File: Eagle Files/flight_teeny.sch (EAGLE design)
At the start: 21 parts, among them M4 WIRELESS-NRF24L01, Q1 SI2302, Q2 SI2302, Q3 SI2302, Q5 SI2302, U2 GY-521MPU6050

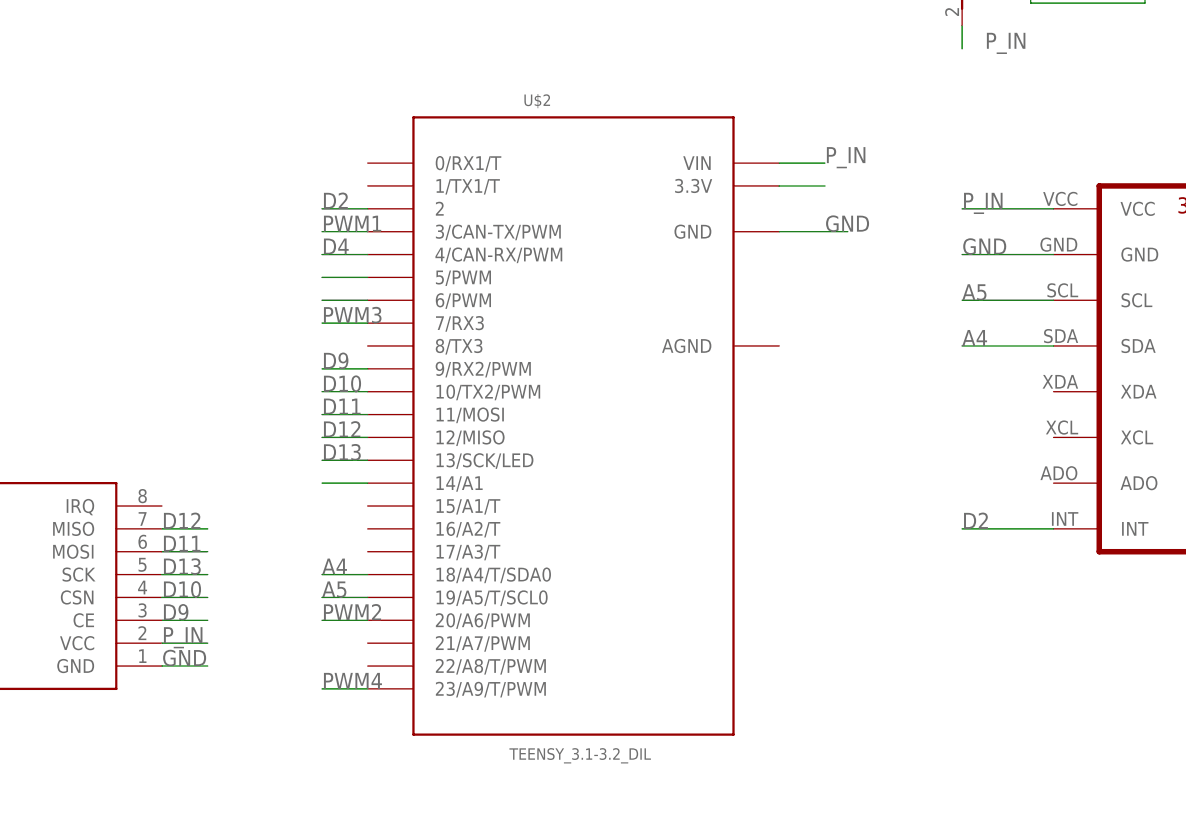
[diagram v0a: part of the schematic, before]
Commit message: Changed power supply for mrf and mpu. Corrected of overlaping pads
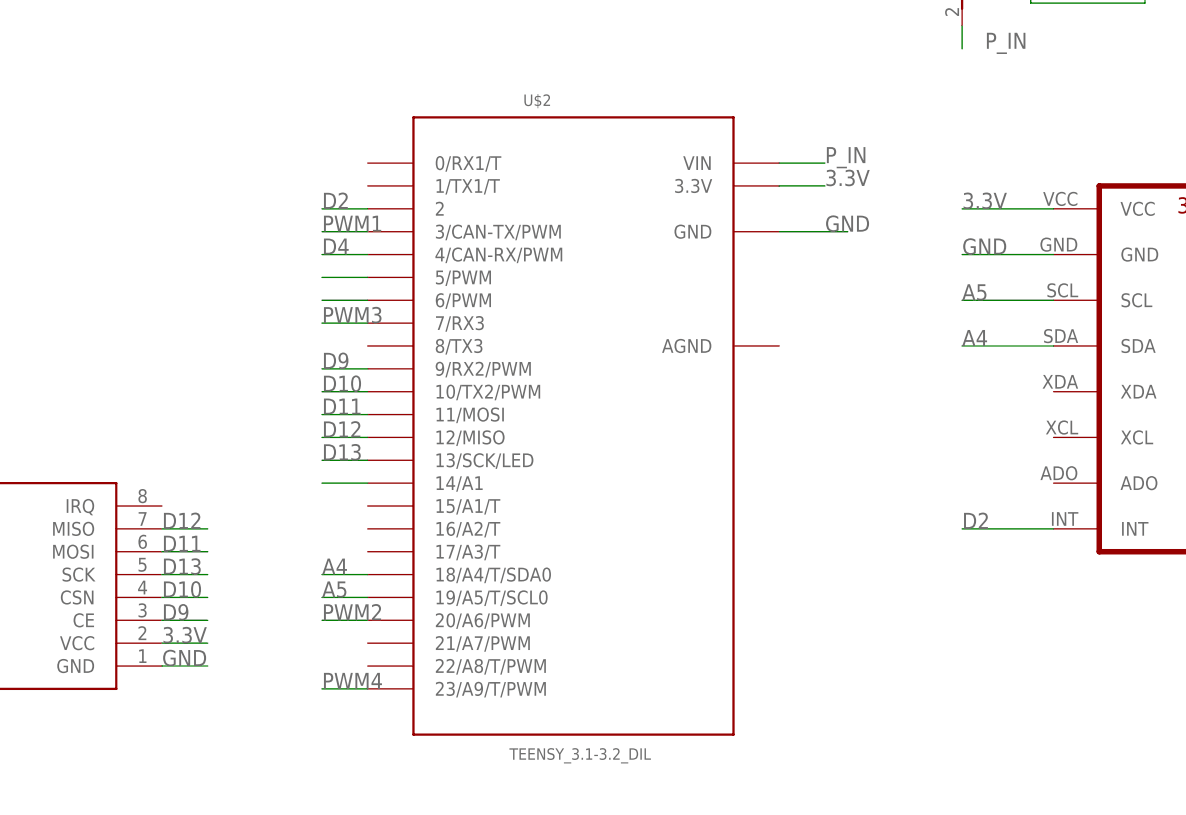
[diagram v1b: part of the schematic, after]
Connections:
- removed net N$10: U$2.3.3V
- new net 3.3V: M4.VCC, U$2.3.3V, U2.VCC
- net P_IN: no longer M4.VCC, U2.VCC
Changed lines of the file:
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@@
 <?xml version="1.0" encoding="utf-8"?>
 <!DOCTYPE eagle SYSTEM "eagle.dtd">
-<eagle version="9.3.2">
+<eagle version="9.2.2">
 <drawing>
 <settings>
@@
 </segment>
 <segment>
+<pinref part="U$2" gate="G$1" pin="VIN"/>
+<wire x1="43.18" y1="-71.12" x2="48.26" y2="-71.12" width="0.1524" layer="91"/>
+<label x="48.26" y="-71.12" size="1.778" layer="95"/>
+</segment>
+</net>
+<net name="N$20" class="0">
+<segment>
+<pinref part="U$2" gate="G$1" pin="14/A1"/>
+<wire x1="-2.54" y1="-106.68" x2="-7.62" y2="-106.68" width="0.1524" layer="91"/>
+</segment>
+</net>
+<net name="3.3V" class="0">
+<segment>
+<pinref part="U$2" gate="G$1" pin="3.3V"/>
+<wire x1="43.18" y1="-73.66" x2="48.26" y2="-73.66" width="0.1524" layer="91"/>
+<label x="48.26" y="-73.66" size="1.778" layer="95"/>
+</segment>
+<segment>
+<pinref part="M4" gate="G$1" pin="VCC"/>
+<wire x1="-25.4" y1="-124.46" x2="-20.32" y2="-124.46" width="0.1524" layer="91"/>
+<label x="-25.4" y="-124.46" size="1.778" layer="95"/>
+</segment>
+<segment>
 <pinref part="U2" gate="G$1" pin="VCC"/>
 <wire x1="73.66" y1="-76.2" x2="63.5" y2="-76.2" width="0.1524" layer="91"/>
 <label x="63.5" y="-76.2" size="1.778" layer="95"/>
 </segment>
-<segment>
-<pinref part="M4" gate="G$1" pin="VCC"/>
-<wire x1="-25.4" y1="-124.46" x2="-20.32" y2="-124.46" width="0.1524" layer="91"/>
-<label x="-25.4" y="-124.46" size="1.778" layer="95"/>
-</segment>
-<segment>
-<pinref part="U$2" gate="G$1" pin="VIN"/>
-<wire x1="43.18" y1="-71.12" x2="48.26" y2="-71.12" width="0.1524" layer="91"/>
-<label x="48.26" y="-71.12" size="1.778" layer="95"/>
-</segment>
-</net>
-<net name="N$20" class="0">
-<segment>
-<pinref part="U$2" gate="G$1" pin="14/A1"/>
-<wire x1="-2.54" y1="-106.68" x2="-7.62" y2="-106.68" width="0.1524" layer="91"/>
-</segment>
-</net>
-<net name="N$10" class="0">
-<segment>
-<pinref part="U$2" gate="G$1" pin="3.3V"/>
-<wire x1="43.18" y1="-73.66" x2="48.26" y2="-73.66" width="0.1524" layer="91"/>
-</segment>
-</net>
+</net>

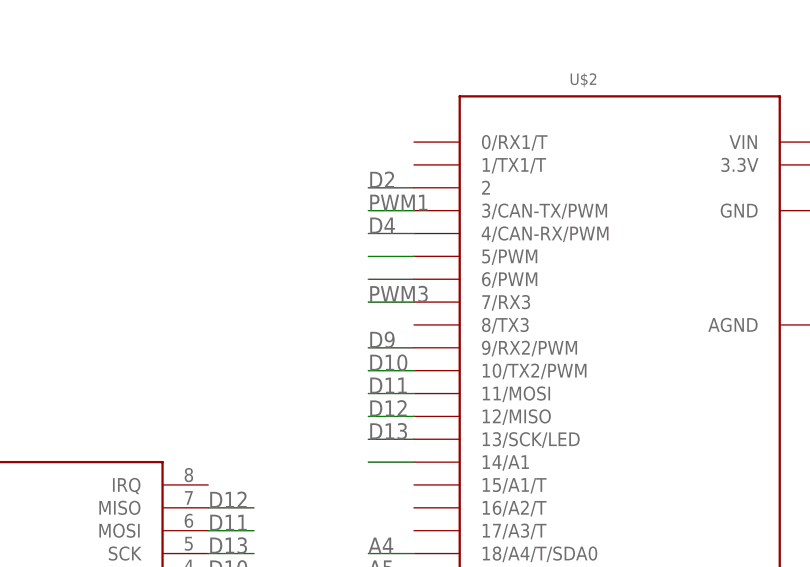
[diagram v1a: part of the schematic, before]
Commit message: PWM pin corrected. Shifted from 7 to 6
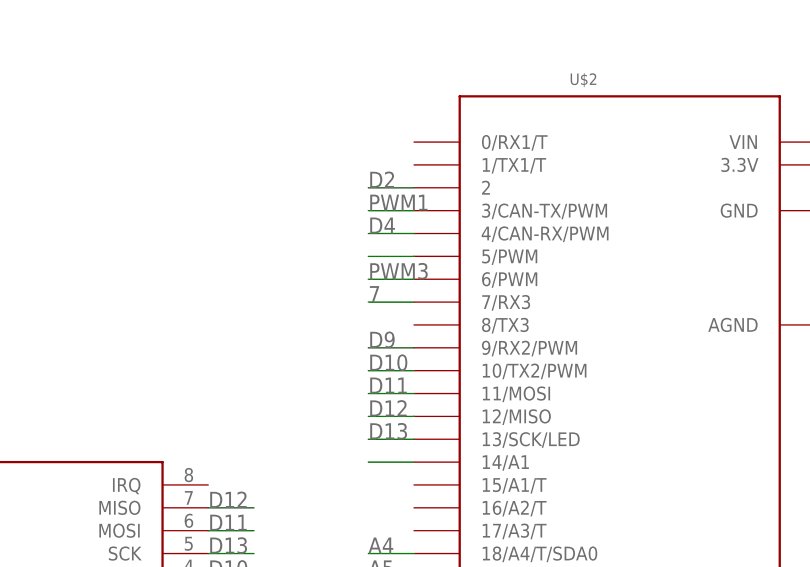
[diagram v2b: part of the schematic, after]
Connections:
- removed net N$3: U$2.6/PWM
- new net 7: U$2.7/RX3
- net PWM3: now also U$2.6/PWM; no longer U$2.7/RX3
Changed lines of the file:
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@@
 </segment>
 <segment>
-<pinref part="U$2" gate="G$1" pin="7/RX3"/>
-<wire x1="-2.54" y1="-88.9" x2="-7.62" y2="-88.9" width="0.1524" layer="91"/>
-<label x="-7.62" y="-88.9" size="1.778" layer="95"/>
+<pinref part="U$2" gate="G$1" pin="6/PWM"/>
+<wire x1="-2.54" y1="-86.36" x2="-7.62" y2="-86.36" width="0.1524" layer="91"/>
+<label x="-7.62" y="-86.36" size="1.778" layer="95"/>
 </segment>
 </net>
@@
 </segment>
 </net>
-<net name="N$3" class="0">
+<net name="7" class="0">
 <segment>
-<pinref part="U$2" gate="G$1" pin="6/PWM"/>
-<wire x1="-2.54" y1="-86.36" x2="-7.62" y2="-86.36" width="0.1524" layer="91"/>
+<pinref part="U$2" gate="G$1" pin="7/RX3"/>
+<wire x1="-2.54" y1="-88.9" x2="-7.62" y2="-88.9" width="0.1524" layer="91"/>
+<label x="-7.62" y="-88.9" size="1.778" layer="95"/>
 </segment>
 </net>
